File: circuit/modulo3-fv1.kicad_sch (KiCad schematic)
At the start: 55 parts, among them J1 CONN_01X04, J2 CONN_01X10, J3 CONN_01X03, J4 HOLE, J5 HOLE, U1 OPA1642, U10 TLE2426, U2 PWR_CONN, U3 FV-1, U5 LM1117 3V3, U7 AD5142A, Y1 32768Hz

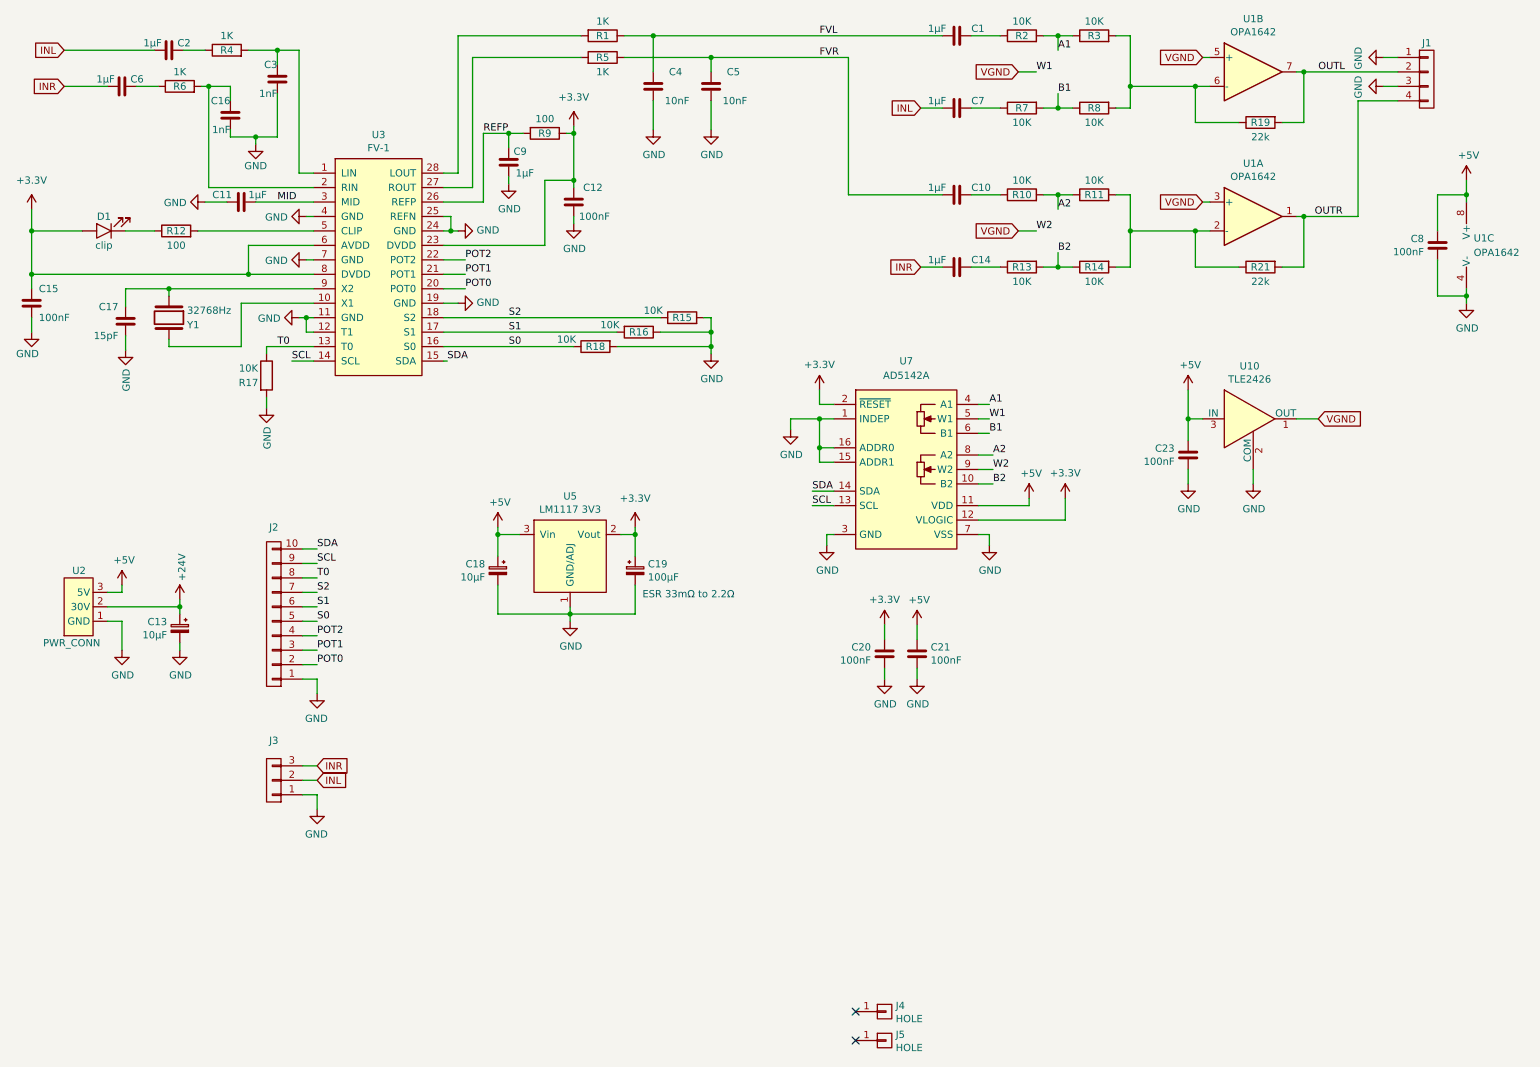
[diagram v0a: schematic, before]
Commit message: mcu board; fv1 board tracing
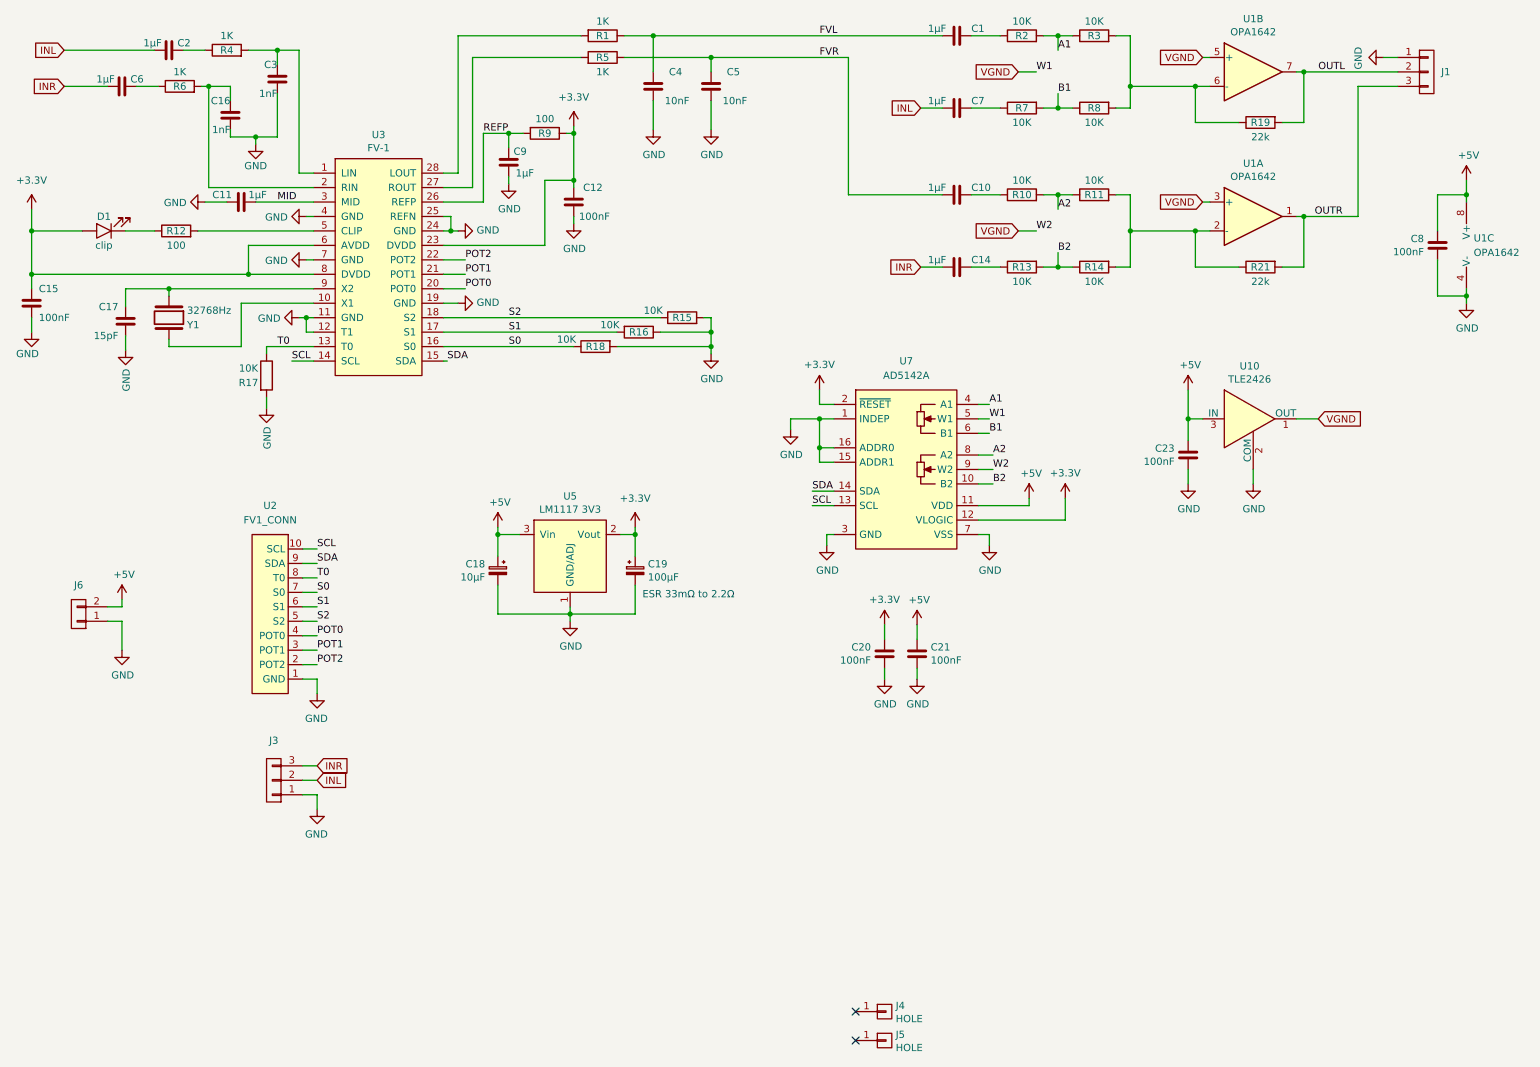
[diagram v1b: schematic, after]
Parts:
- removed C13: 10µF, myAmp:CPOL_D6.3_P2.5, symbol myAmp:CPOL
- removed J1: CONN_01X04, myAmp:PIN_1x04, symbol myAmp:CONN_01X04
- removed J2: CONN_01X10, myAmp:PIN_1x10, symbol myAmp:CONN_01X10
- removed U2: PWR_CONN, myAmp:PWR_CONN, symbol myAmp:PWR_CONN
- added J1: CONN_01X03, myAmp:PIN_1x03, symbol myAmp:CONN_01X03
- added J6: CONN_01X02, myAmp:PIN_1x02, symbol myAmp:CONN_01X02
- added U2: FV1_CONN, myAmp:PIN_1x10, symbol myAmp:FV1_CONN
- R1, R10, R11, R13, R14, R19, R2, R21, R3, R5, R7, R8: footprint myAmp:R_1206 -> myAmp:R_10MM
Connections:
- net +5V: now also J6.2 (P2)
- net GND: now also J1.1, J6.1 (P1), U2.1 (GND)
- net OUTL: now also J1.2
- net OUTR: now also J1.3
- net POT0: now also U2.4 (POT0)
- net POT1: now also U2.3 (POT1)
- net POT2: now also U2.2 (POT2)
- net S0: now also U2.7 (S0)
- net S1: now also U2.6 (S1)
- net S2: now also U2.5 (S2)
- net SCL: now also U2.10 (SCL)
- net SDA: now also U2.9 (SDA)
- net T0: now also U2.8 (T0)

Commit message: general layout and board sizes
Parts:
- U2: footprint myAmp:PIN_1x10 -> myAmp:FV1_CONN
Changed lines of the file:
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@@
     (property "Reference" "U2" (id 0) (at 59.69 99.06 0))
     (property "Value" "FV1_CONN" (id 1) (at 59.69 101.6 0))
-    (property "Footprint" "myAmp:PIN_1x10" (id 2) (at 65.405 137.16 0)
+    (property "Footprint" "myAmp:FV1_CONN" (id 2) (at 65.405 137.16 0)
       (effects (font (size 1.27 1.27)) hide)
     )
@@
     )
     (path "/7ecda2af-480d-4b2d-8eae-09c8c67a1787"
-      (reference "U2") (unit 1) (value "FV1_CONN") (footprint "myAmp:PIN_1x10")
+      (reference "U2") (unit 1) (value "FV1_CONN") (footprint "myAmp:FV1_CONN")
     )
     (path "/00000000-0000-0000-0000-00005ef23204"

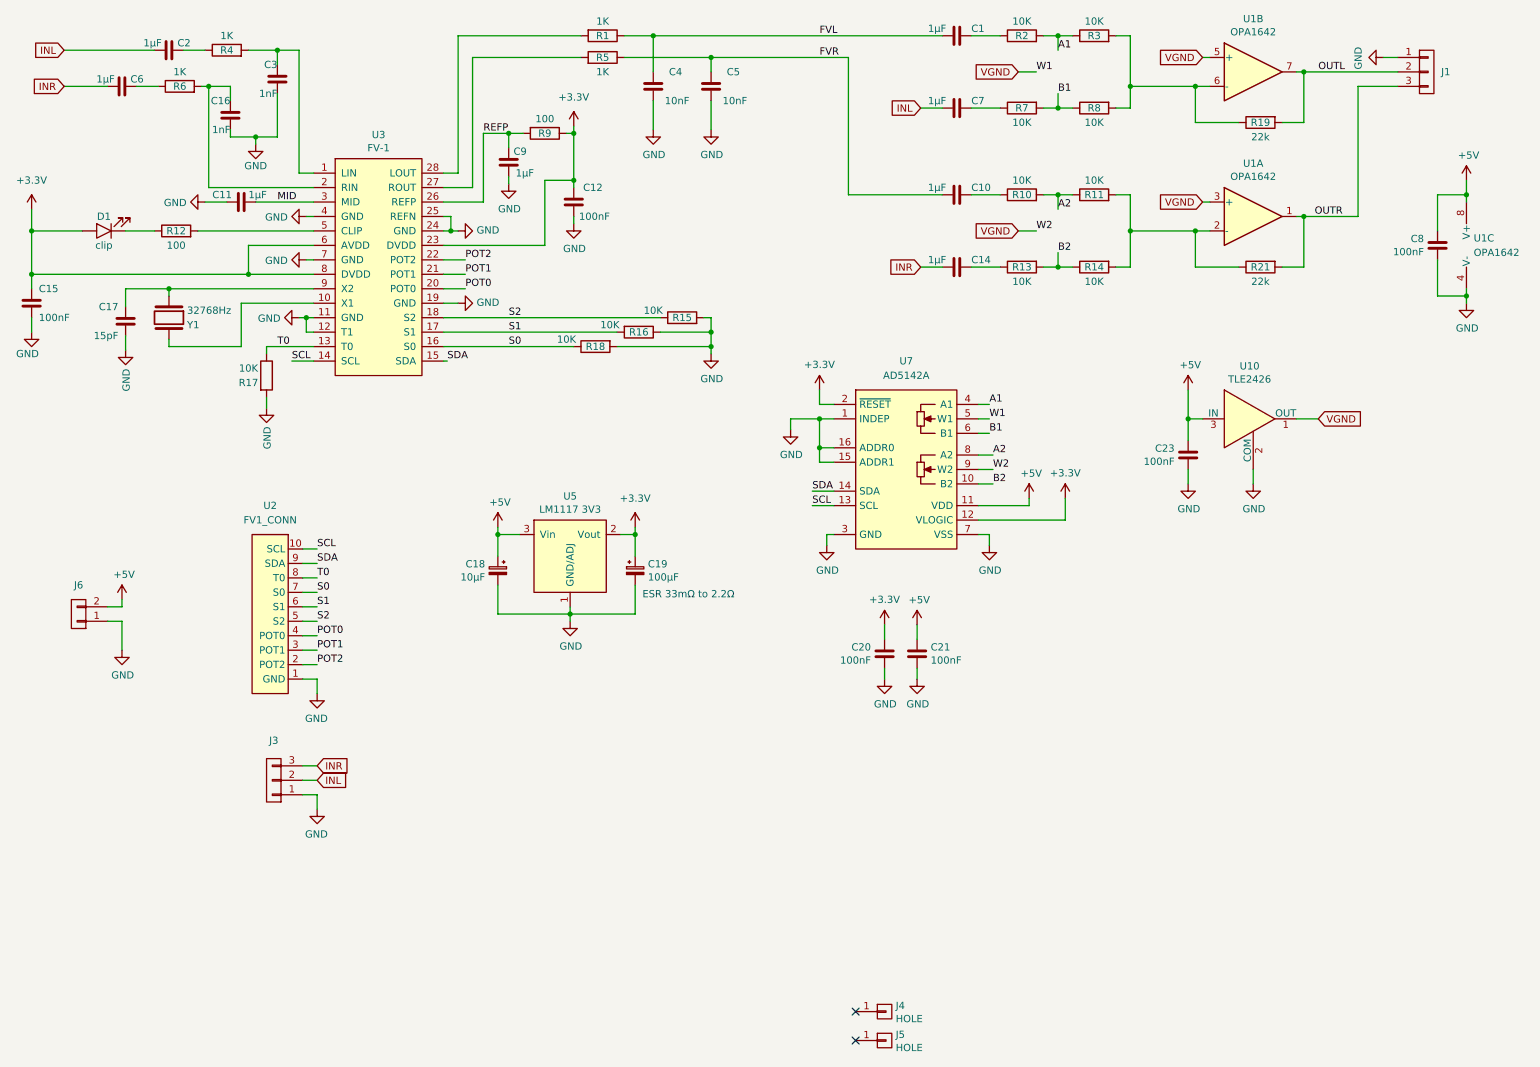
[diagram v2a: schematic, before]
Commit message: got the pcs and holes sizes for mcu, poweamp and fv1
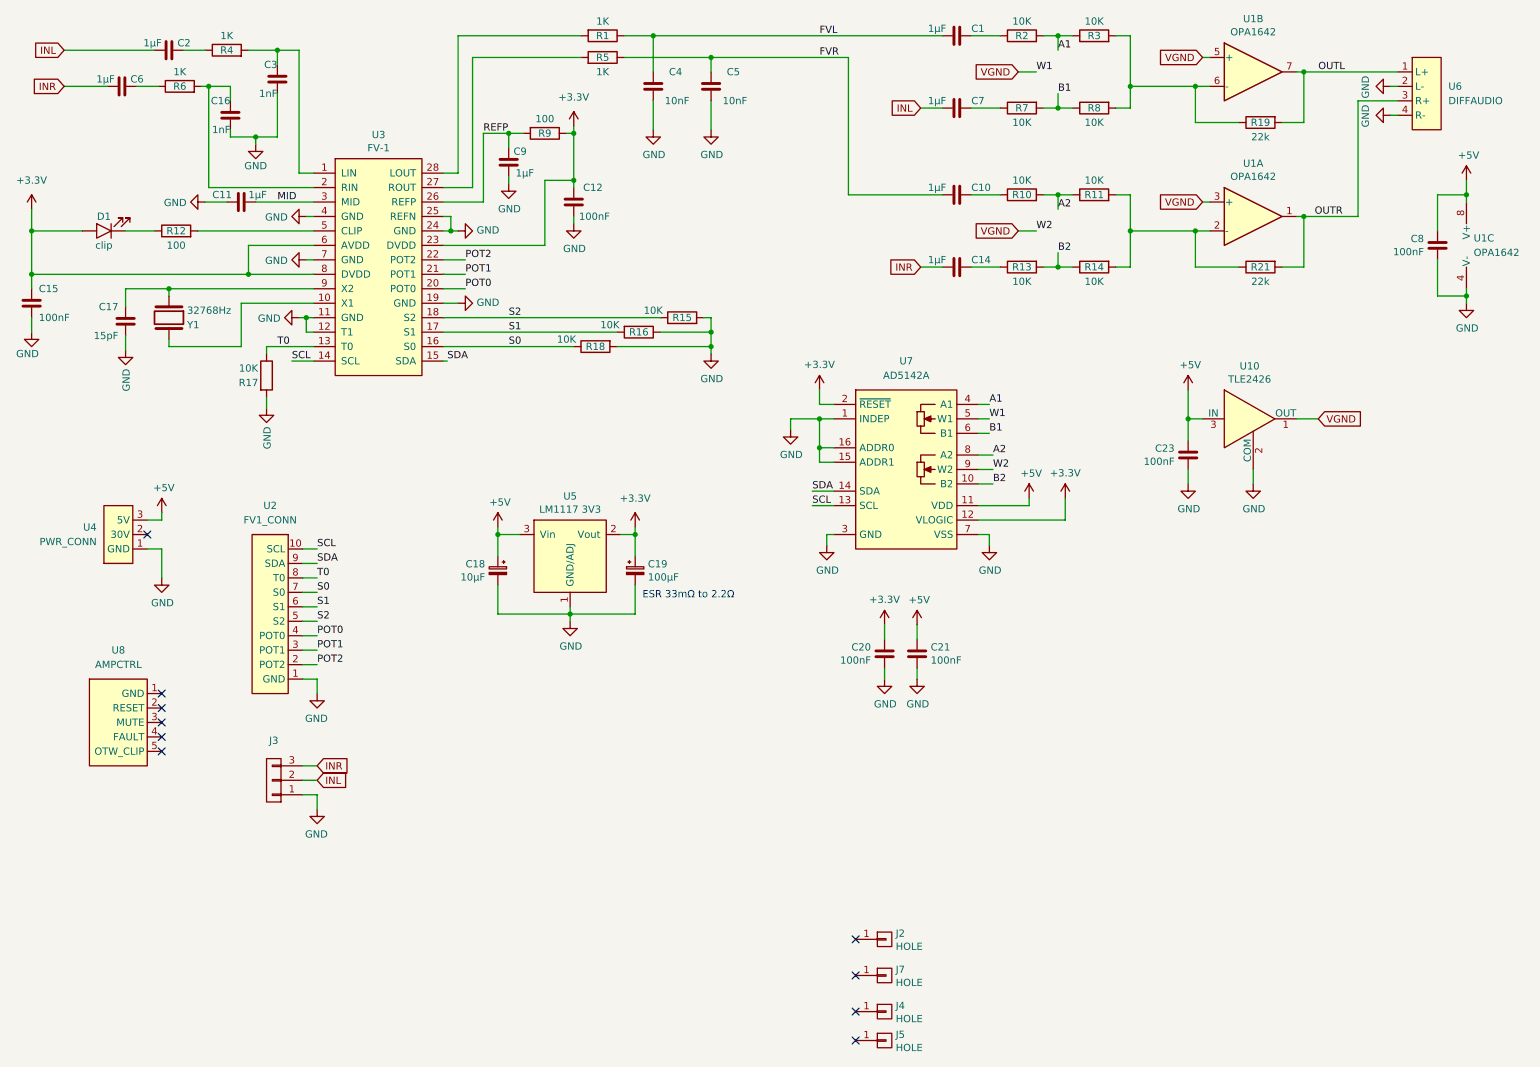
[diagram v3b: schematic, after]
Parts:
- removed J1: CONN_01X03, myAmp:PIN_1x03, symbol myAmp:CONN_01X03
- removed J6: CONN_01X02, myAmp:PIN_1x02, symbol myAmp:CONN_01X02
- added J2, J7: HOLE, myAmp:MountingHole, symbol myAmp:HOLE
- added U4: PWR_CONN, myAmp:PWR_CONN, symbol myAmp:PWR_CONN
- added U6: DIFFAUDIO, myAmp:DIFFAUDIO, symbol myAmp:DIFFAUDIO
- added U8: AMPCTRL, myAmp:AMPCTRL, symbol myAmp:AMPCTRL
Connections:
- net +5V: now also U4.3 (5V)
- net GND: now also U4.1 (GND), U6.2 (L-), U6.4 (R-)
- net OUTL: now also U6.1 (L+)
- net OUTR: now also U6.3 (R+)
- no-connect marks 2 -> 10

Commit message: fv-1 mostly done; power progressed
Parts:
- removed J3: CONN_01X03, myAmp:PIN_1x03, symbol myAmp:CONN_01X03
- added U9: PREAMP, myAmp:PREAMP_CONN, symbol myAmp:PREAMP_CONN
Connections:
- net GND: now also U8.1 (GND), U9.3 (GND); no longer U2.1 (GND)
- net INL: now also U9.5 (LEFT)
- net INR: now also U9.6 (RIGHT)
- net POT0: now also U2.3 (POT0); no longer U2.4 (POT0)
- net POT1: now also U2.2 (POT1); no longer U2.3 (POT1)
- net POT2: now also U2.1 (POT2); no longer U2.2 (POT2)
- net S0: now also U2.6 (S0); no longer U2.7 (S0)
- net S1: now also U2.5 (S1); no longer U2.6 (S1)
- net S2: now also U2.4 (S2); no longer U2.5 (S2)
- net SCL: now also U9.2 (SCL); no longer U2.10 (SCL), U3.14 (SCL)
- net SDA: now also U9.1 (SDA); no longer U2.9 (SDA), U3.15 (SDA)
- net T0: now also U2.9 (T0); no longer U2.8 (T0)
- net CLIP: now reaches R12.2, U3.5 (CLIP)
- net CLIP: now also U2.10 (CLP)
- net 30V: now reaches U4.2 (30V)
- net 30V: now also U9.4 (30V)
- new net FV_SCL: U2.8 (SCL), U3.14 (SCL)
- new net FV_SDA: U2.7 (SDA), U3.15 (SDA)
- no-connect marks 10 -> 4
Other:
- moved on the sheet: C18, R17, U2
